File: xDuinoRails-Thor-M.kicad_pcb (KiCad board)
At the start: 6 copper layers, 30 x 20.1 mm, 46 parts, among them J701 Conn_02x11_Odd_Even, Q501 S8050, Q601 S8550, Q602 S8550, Q604 S8050, Q901 BSS138, Q902 BSS138, U1101 MOUDLE-SEEEDUINO-XIAO, U201 HT75xx-1-SOT89, U801 BDR6133

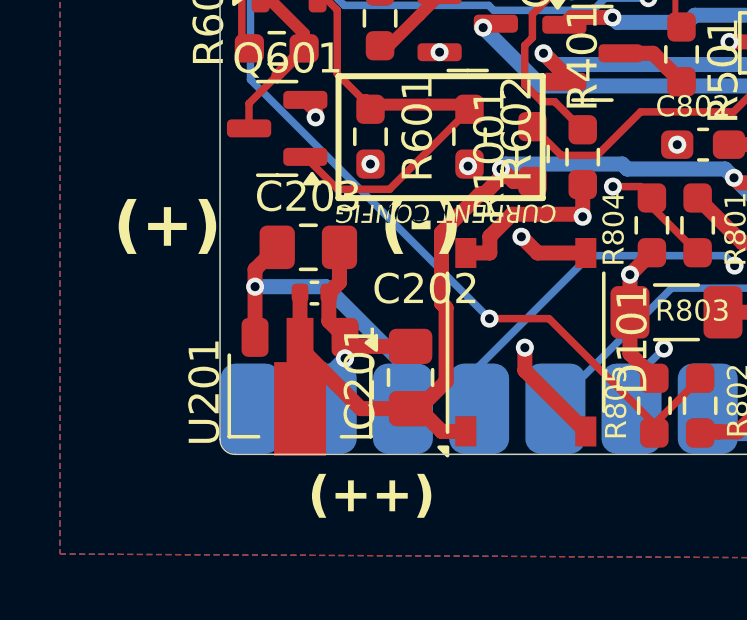
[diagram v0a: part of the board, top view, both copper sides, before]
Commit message: Fix - Yellow background on subcircuits
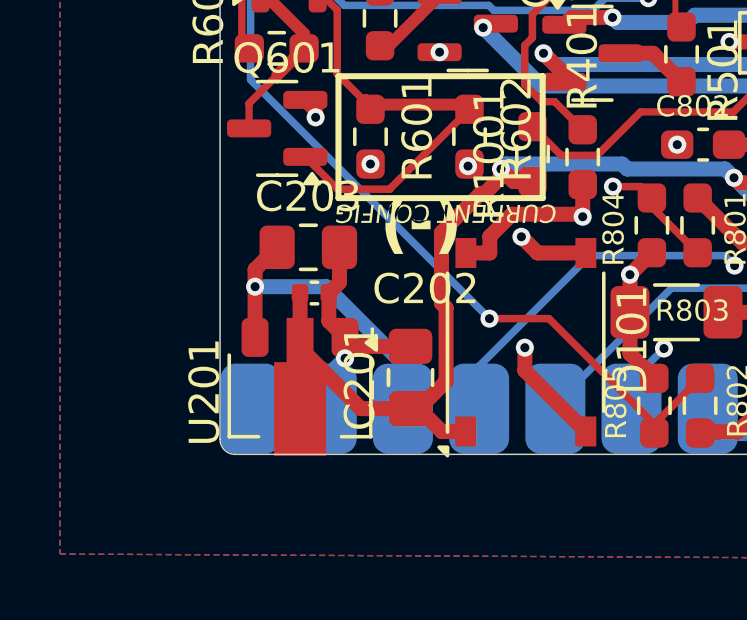
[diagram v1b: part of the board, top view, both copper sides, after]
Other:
- board text removed: "(+)"
- board text removed: "(++)"
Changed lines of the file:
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@@
 		)
 	)
-	(gr_text "(+)"
-		(at 139.446 101.0495 180)
-		(layer "F.SilkS")
-		(effects
-			(font
-				(size 1.5 1.5)
-				(thickness 0.3)
-				(bold yes)
-			)
-			(justify left bottom mirror)
-		)
-	)
 	(gr_text "(-)"
 		(at 148.336 101.0495 180)
@@
 		)
 	)
-	(gr_text "(++)"
-		(at 145.923 110.1935 180)
-		(layer "F.SilkS")
-		(effects
-			(font
-				(size 1.2 1.2)
-				(thickness 0.3)
-				(bold yes)
-			)
-			(justify left bottom mirror)
-		)
-	)
 	(gr_text "Fehlender PIN"
 		(at 170.688 109.22 0)
@@
 	(group "subpcb_Stammblatt/rails_power_dc-dc-ldo-3v3_100mA"
 		(members "2495a32d-55d5-45c7-bf0d-90cec6114754" "8e28e822-f441-4a15-be24-b48dd8eb495f"
-			"b21880ad-efed-4d92-a443-c5eb617b914d" "f0e60a2e-b953-45e2-a762-24d2fcbf639e"
-			"f9515013-ffaf-46c4-ab7f-0578365a6d72" "fb06f133-c07a-4c25-8496-d953793c34f3"
+			"f0e60a2e-b953-45e2-a762-24d2fcbf639e" "f9515013-ffaf-46c4-ab7f-0578365a6d72"
 		)
 	)
